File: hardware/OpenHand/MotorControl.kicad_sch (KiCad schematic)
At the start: 52 parts, among them U10 DRV8833PWP, U11 DRV8833PWP, U12 DRV8833PWP, U13 DRV8833PWP

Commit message: Major updates to schm and pcb, a bit better design
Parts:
- C28: renamed from C27; footprint Capacitor_SMD:C_0805_2012Metric_Pad1.18x1.45mm_HandSolder -> Capacitor_SMD:C_0805_2012Metric
- C29: renamed from C28; footprint Capacitor_SMD:C_0805_2012Metric_Pad1.18x1.45mm_HandSolder -> Capacitor_SMD:C_0805_2012Metric
- C30: renamed from C29; footprint Capacitor_SMD:C_0805_2012Metric_Pad1.18x1.45mm_HandSolder -> Capacitor_SMD:C_0805_2012Metric
- C31: renamed from C30; footprint Capacitor_SMD:C_0805_2012Metric_Pad1.18x1.45mm_HandSolder -> Capacitor_SMD:C_0805_2012Metric
- C32: renamed from C31; footprint Capacitor_SMD:C_0805_2012Metric_Pad1.18x1.45mm_HandSolder -> Capacitor_SMD:C_0805_2012Metric
- C33: renamed from C32; footprint Capacitor_SMD:C_0805_2012Metric_Pad1.18x1.45mm_HandSolder -> Capacitor_SMD:C_0805_2012Metric
- C34: renamed from C33; footprint Capacitor_SMD:C_0805_2012Metric_Pad1.18x1.45mm_HandSolder -> Capacitor_SMD:C_0805_2012Metric
- C35: renamed from C34; footprint Capacitor_SMD:C_0805_2012Metric_Pad1.18x1.45mm_HandSolder -> Capacitor_SMD:C_0805_2012Metric
- C36: renamed from C35; footprint Capacitor_SMD:C_0805_2012Metric_Pad1.18x1.45mm_HandSolder -> Capacitor_SMD:C_0805_2012Metric
- C37: renamed from C36; footprint Capacitor_SMD:C_0805_2012Metric_Pad1.18x1.45mm_HandSolder -> Capacitor_SMD:C_0805_2012Metric
- C38: renamed from C37; footprint Capacitor_SMD:C_0805_2012Metric_Pad1.18x1.45mm_HandSolder -> Capacitor_SMD:C_0805_2012Metric
- C39: renamed from C38; footprint Capacitor_SMD:C_0805_2012Metric_Pad1.18x1.45mm_HandSolder -> Capacitor_SMD:C_0805_2012Metric
- R52: renamed from R56; footprint Resistor_SMD:R_1206_3216Metric_Pad1.30x1.75mm_HandSolder -> Resistor_SMD:R_0805_2012Metric
- R53: renamed from R57; footprint Resistor_SMD:R_1206_3216Metric_Pad1.30x1.75mm_HandSolder -> Resistor_SMD:R_0805_2012Metric
- R54: renamed from R58; footprint Resistor_SMD:R_1206_3216Metric_Pad1.30x1.75mm_HandSolder -> Resistor_SMD:R_1206_3216Metric
- R55: renamed from R59; footprint Resistor_SMD:R_1206_3216Metric_Pad1.30x1.75mm_HandSolder -> Resistor_SMD:R_1206_3216Metric
- R56: renamed from R60; footprint Resistor_SMD:R_1206_3216Metric_Pad1.30x1.75mm_HandSolder -> Resistor_SMD:R_0805_2012Metric
- R57: renamed from R61; footprint Resistor_SMD:R_1206_3216Metric_Pad1.30x1.75mm_HandSolder -> Resistor_SMD:R_0805_2012Metric
- R58: renamed from R62; footprint Resistor_SMD:R_1206_3216Metric_Pad1.30x1.75mm_HandSolder -> Resistor_SMD:R_1206_3216Metric
- R59: renamed from R63; footprint Resistor_SMD:R_1206_3216Metric_Pad1.30x1.75mm_HandSolder -> Resistor_SMD:R_1206_3216Metric
- R60: renamed from R64; footprint Resistor_SMD:R_1206_3216Metric_Pad1.30x1.75mm_HandSolder -> Resistor_SMD:R_1206_3216Metric
- renumbered TP53 to TP30, TP54 to TP31, TP55 to TP32, TP56 to TP33, TP57 to TP34, TP58 to TP35, TP59 to TP36, TP60 to TP37, TP61 to TP38, TP62 to TP39, TP63 to TP40, TP64 to TP41, TP65 to TP42, TP66 to TP43, TP67 to TP44, TP68 to TP45, TP69 to TP46, TP70 to TP47, TP71 to TP48, TP72 to TP49, TP73 to TP50, TP74 to TP51, TP75 to TP52, TP76 to TP53, TP77 to TP54, TP78 to TP55, TP79 to TP56, U13 to U10, U10 to U7, U11 to U8, U12 to U9
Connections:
- net FDBK_MOTOR_1_N renamed HAPTIC_01_N
- net FDBK_MOTOR_1_P renamed HAPTIC_01_P
- net FDBK_MOTOR_1_UC1 renamed HAPTIC_01_DIR
- net FDBK_MOTOR_1_UC2 renamed HAPTIC_01_PWM
- net FDBK_MOTOR_2_N renamed HAPTIC_02_N
- net FDBK_MOTOR_2_P renamed HAPTIC_02_P
- net FDBK_MOTOR_2_UC1 renamed HAPTIC_02_DIR
- net FDBK_MOTOR_2_UC2 renamed HAPTIC_02_PWM
- net FDBK_MOTOR_EN renamed HAPTIC_EN
- net FDBK_MOTOR_FAULT renamed HAPTIC_FAULT
- net MOTOR_1_EN renamed MOTOR_01_EN
- net MOTOR_1_FAULT renamed MOTOR_01_FAULT
- net MOTOR_1_N renamed MOTOR_01_N
- net MOTOR_1_P renamed MOTOR_01_P
- net MOTOR_1_UC1 renamed MOTOR_01_DIR
- net MOTOR_1_UC2 renamed MOTOR_01_PWM
- net MOTOR_2_EN renamed MOTOR_02_EN
- net MOTOR_2_FAULT renamed MOTOR_02_FAULT
- net MOTOR_2_N renamed MOTOR_02_N
- net MOTOR_2_P renamed MOTOR_02_P
- net MOTOR_2_UC1 renamed MOTOR_02_DIR
- net MOTOR_2_UC2 renamed MOTOR_02_PWM
- net MOTOR_3_EN renamed MOTOR_03_EN
- net MOTOR_3_FAULT renamed MOTOR_03_FAULT
- net MOTOR_3_N renamed MOTOR_03_N
- net MOTOR_3_P renamed MOTOR_03_P
- net MOTOR_3_UC1 renamed MOTOR_03_DIR
- net MOTOR_3_UC2 renamed MOTOR_03_PWM
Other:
- note added: "Using PWM and GPIO signals on pins xIN1 and xIN2, we can control the speed (current) and direction of connected DC motors. Looking at the datasheet, we can use xIN2 as PWM for speed, and xIN1 as direction input (HIGH for forward, LOW for reverse). PWM frequency should be 50kHz. When the voltage on pin xISEN exceeds VTRIP (0.2 V), current regulation is activated. The RISENSE resistor should be siz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"
- note removed: "Using PWM and GPIO signals on pins xIN1 and xIN2, we can control the speed (current) and direction of connected DC motors. Looking at the datasheet, we can use xIN1 as PWM for speed, and xIN2 as direction input (HIGH for reverse, LOW for forward). PWM frequency should be 50kHz. When the voltage on pin xISEN exceeds VTRIP (0.2 V), current regulation is activated. The RISENSE resistor should be siz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"
- moved on the sheet: TP36, TP37, TP38, TP39

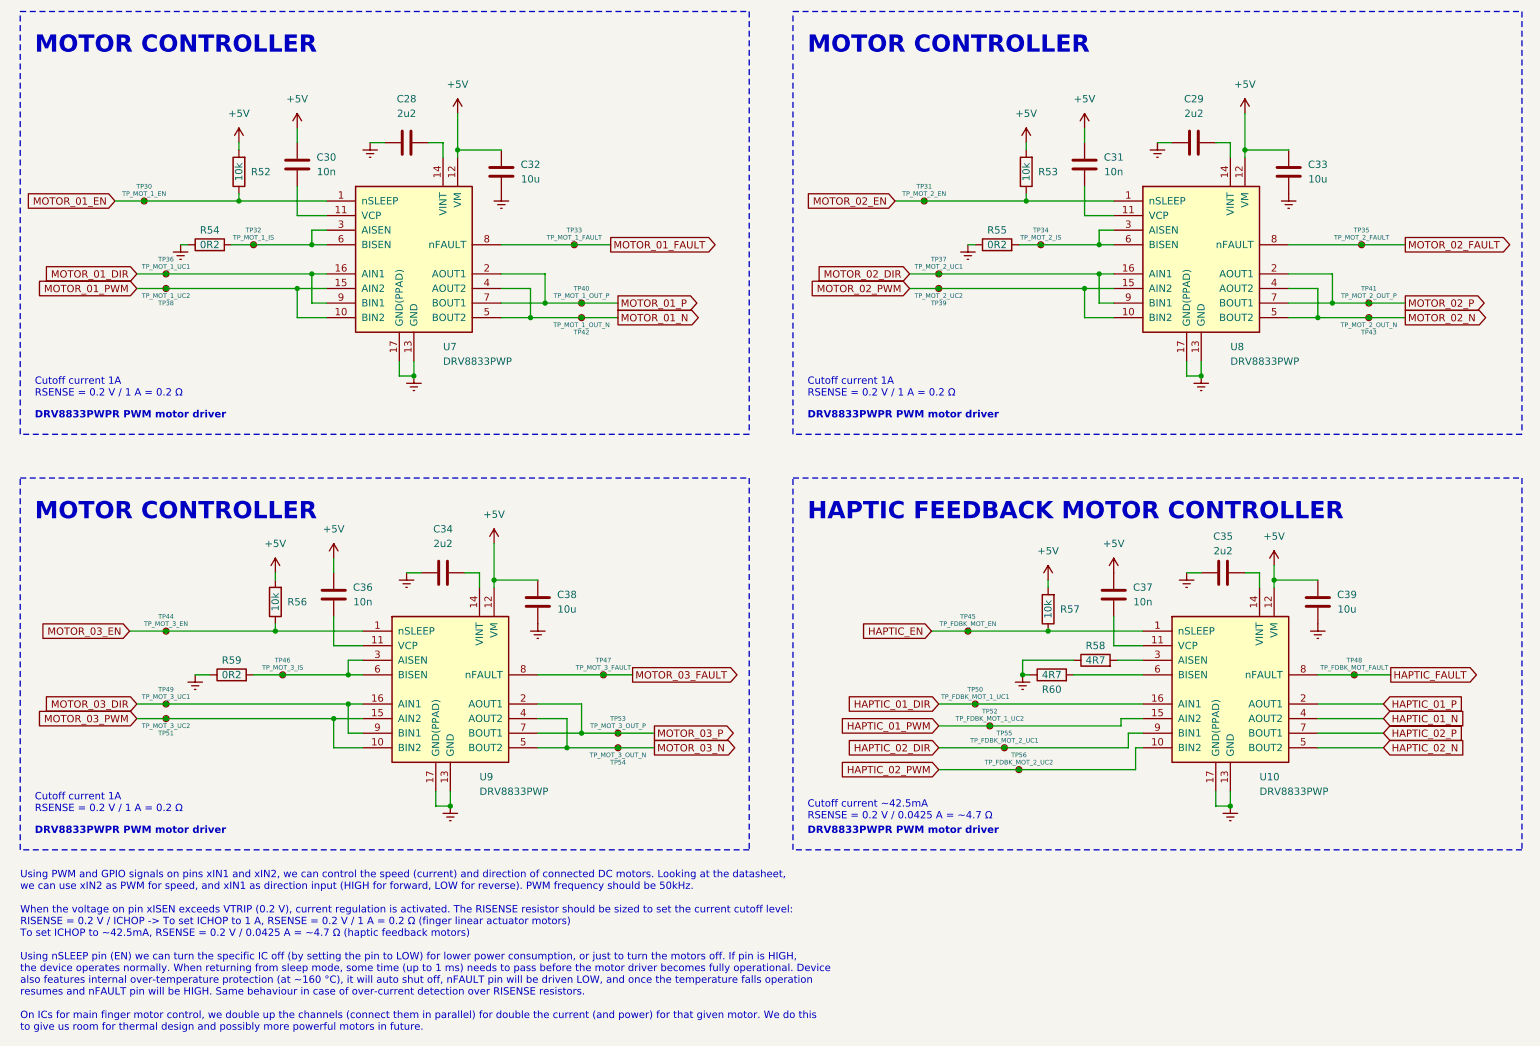
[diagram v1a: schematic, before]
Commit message: Update PCB, add STLs from hand model
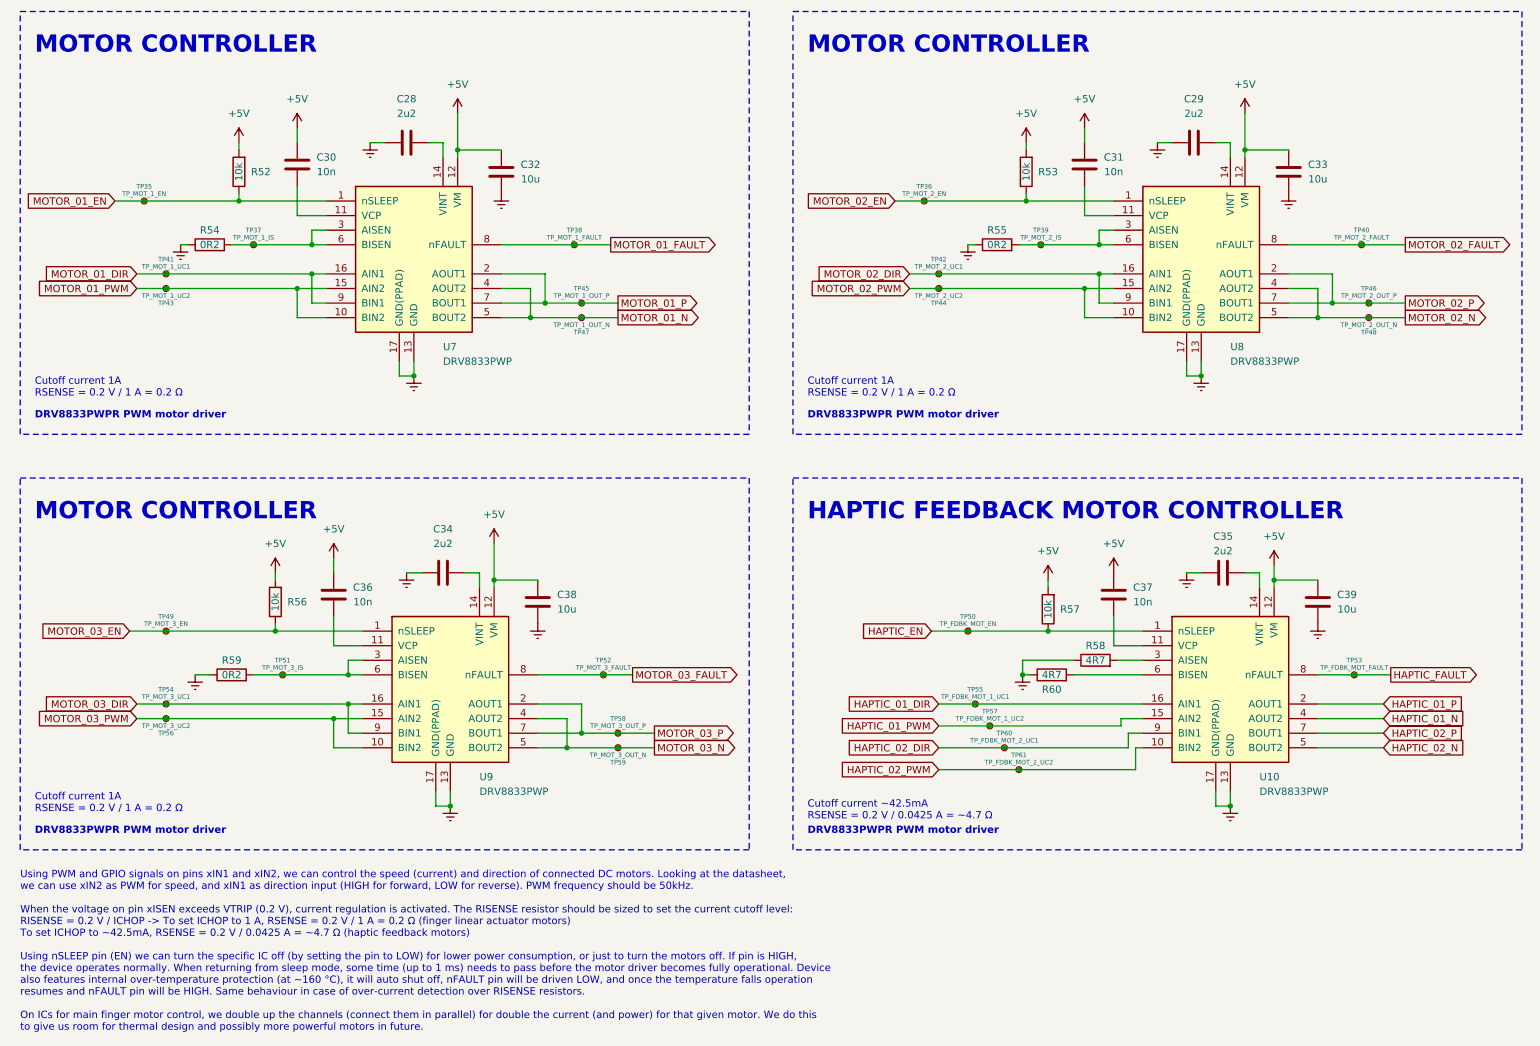
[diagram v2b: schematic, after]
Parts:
- renumbered TP30 to TP35, TP31 to TP36, TP32 to TP37, TP33 to TP38, TP34 to TP39, TP35 to TP40, TP36 to TP41, TP37 to TP42, TP38 to TP43, TP39 to TP44, TP40 to TP45, TP41 to TP46, TP42 to TP47, TP43 to TP48, TP44 to TP49, TP45 to TP50, TP46 to TP51, TP47 to TP52, TP48 to TP53, TP49 to TP54, TP50 to TP55, TP51 to TP56, TP52 to TP57, TP53 to TP58, TP54 to TP59, TP55 to TP60, TP56 to TP61
